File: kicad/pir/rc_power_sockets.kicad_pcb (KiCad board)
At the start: 2 copper layers, 50 x 50 mm, 31 parts, among them IC1 ATTINY85, J1 PIR, J2 433MHZ, J3 433MHZ, P1 ICSP, P2 ALT_PWR, Q1 NMOS, Q2 PMOS, U1 MCP1755ST-3302E/DB

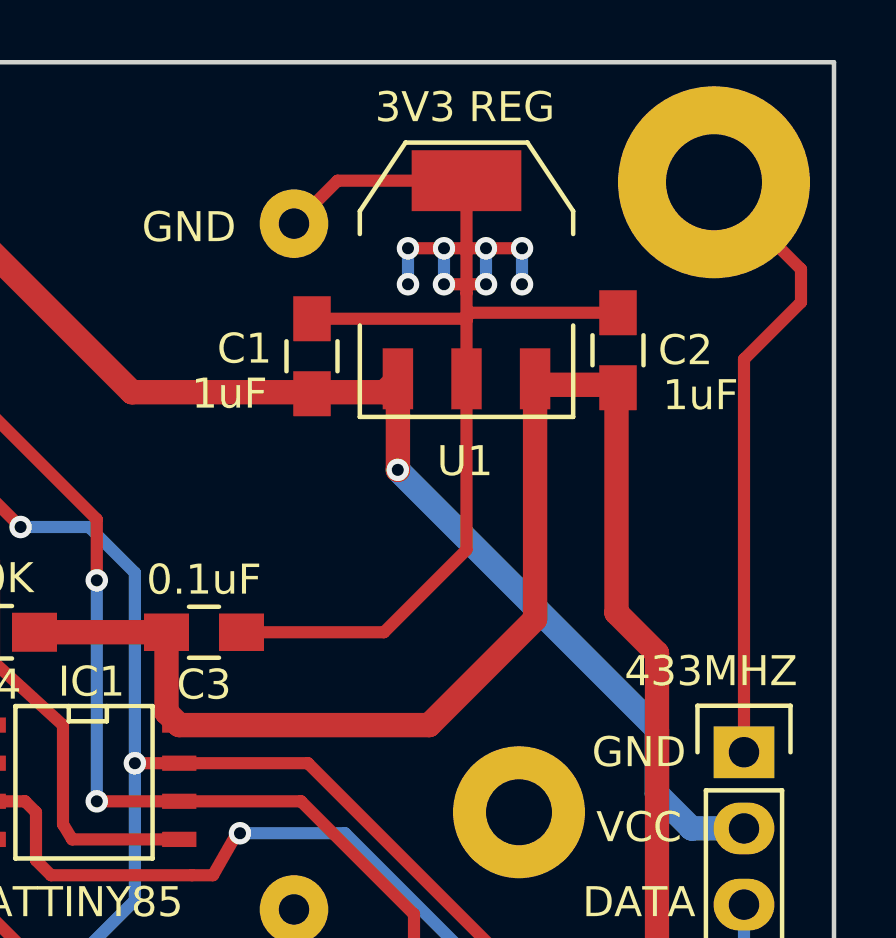
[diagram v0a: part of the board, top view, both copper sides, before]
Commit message: Moved cap away from mounting hole
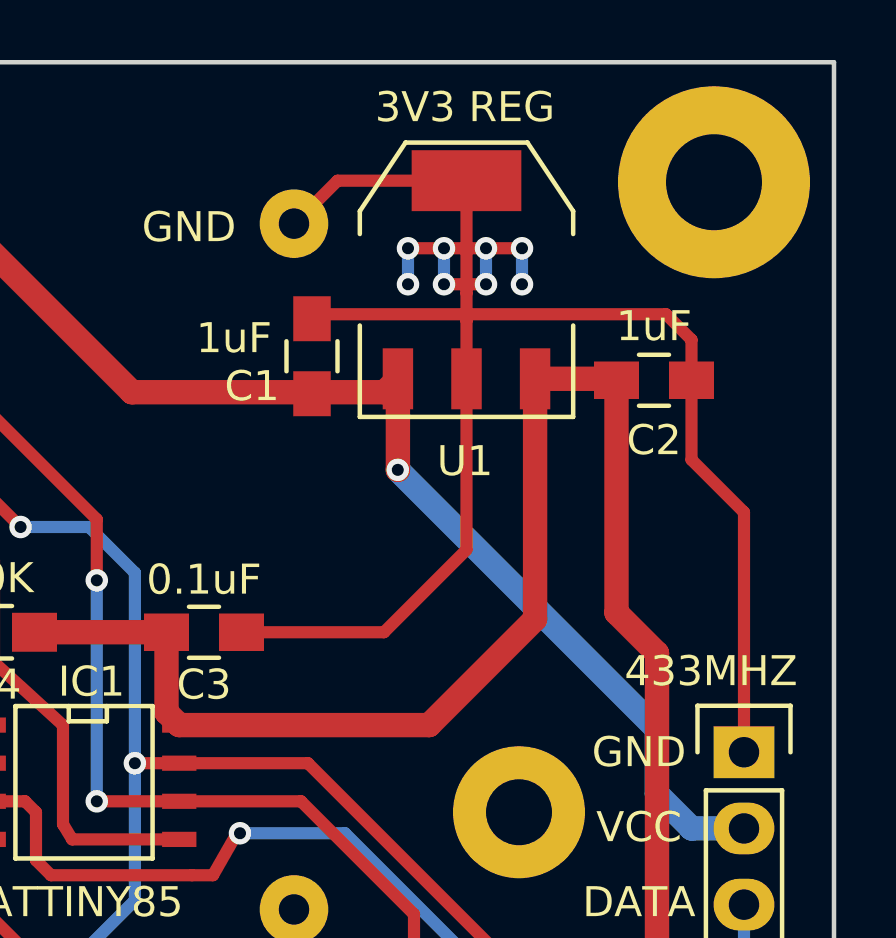
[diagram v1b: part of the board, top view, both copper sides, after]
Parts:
- moved C2 1.56 mm to (164.0, 70.6), turned to 0 degrees
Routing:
- net GND: track 209.1 -> 205.8 mm
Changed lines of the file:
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@@
-(kicad_pcb (version 4) (host pcbnew 4.0.1-stable)
+(kicad_pcb (version 4) (host pcbnew 4.0.2-4+6225~38~ubuntu14.04.1-stable)
   (general
     (links 56)
@@
     (thickness 1.6)
     (drawings 40)
-    (tracks 233)
+    (tracks 235)
     (zones 0)
     (modules 31)
@@
     (tags "capacitor 0805")
     (attr smd)
-    (fp_text reference C1 (at 0.25 -2.25 360) (layer F.SilkS)
-      (effects (font (size 1 1) (thickness 0.15)))
-    )
-    (fp_text value 1uF (at -1.25 -2.75 360) (layer F.SilkS)
+    (fp_text reference C1 (at -1 -2 360) (layer F.SilkS)
+      (effects (font (size 1 1) (thickness 0.15)))
+    )
+    (fp_text value 1uF (at 0.6 -2.6 360) (layer F.SilkS)
       (effects (font (size 1 1) (thickness 0.15)))
     )
@@
   )
   (module Capacitors_SMD:C_0805_HandSoldering (layer F.Cu)
-    (at 162.8 69.6 90)
+    (at 164 70.6)
     (descr "Capacitor SMD 0805, hand soldering")
     (tags "capacitor 0805")
     (attr smd)
-    (fp_text reference C2 (at 0 2.25 360) (layer F.SilkS)
-      (effects (font (size 1 1) (thickness 0.15)))
-    )
-    (fp_text value 1uF (at -1.5 2.75 180) (layer F.SilkS)
+    (fp_text reference C2 (at 0 2) (layer F.SilkS)
+      (effects (font (size 1 1) (thickness 0.15)))
+    )
+    (fp_text value 1uF (at 0 -1.8 180) (layer F.SilkS)
       (effects (font (size 1 1) (thickness 0.15)))
     )
@@
     (fp_line (start 0.5 -0.85) (end -0.5 -0.85) (layer F.SilkS) (width 0.15))
     (fp_line (start -0.5 0.85) (end 0.5 0.85) (layer F.SilkS) (width 0.15))
-    (pad 1 smd rect (at -1.25 0 90) (size 1.5 1.25) (layers F.Cu F.Paste F.Mask)
+    (pad 1 smd rect (at -1.25 0) (size 1.5 1.25) (layers F.Cu F.Paste F.Mask)
       (net 9 /3.3v))
-    (pad 2 smd rect (at 1.25 0 90) (size 1.5 1.25) (layers F.Cu F.Paste F.Mask)
+    (pad 2 smd rect (at 1.25 0) (size 1.5 1.25) (layers F.Cu F.Paste F.Mask)
       (net 1 GND))
     (model Capacitors_SMD.3dshapes/C_0805_HandSoldering.wrl
@@
   (gr_line (start 170 60) (end 170 110) (angle 90) (layer Edge.Cuts) (width 0.15))
   (gr_line (start 120 60) (end 170 60) (angle 90) (layer Edge.Cuts) (width 0.15))
+  (segment (start 157.8 68.4) (end 152.75 68.4) (width 0.406) (layer F.Cu) (net 1) (status 800000))
+  (segment (start 152.75 68.4) (end 152.6 68.55) (width 0.406) (layer F.Cu) (net 1) (status C00000))
+  (segment (start 165.25 70.6) (end 165.25 69.25) (width 0.406) (layer F.Cu) (net 1) (status 400000))
+  (segment (start 164.4 68.4) (end 157.8 68.4) (width 0.406) (layer F.Cu) (net 1))
+  (segment (start 157.8 68.4) (end 157.75 68.4) (width 0.406) (layer F.Cu) (net 1))
+  (segment (start 165.25 69.25) (end 164.4 68.4) (width 0.406) (layer F.Cu) (net 1))
+  (segment (start 167 83) (end 167 75) (width 0.406) (layer F.Cu) (net 1))
+  (segment (start 167 75) (end 165.25 73.25) (width 0.406) (layer F.Cu) (net 1))
+  (segment (start 165.25 73.25) (end 165.25 70.6) (width 0.406) (layer F.Cu) (net 1))
   (segment (start 157 66.2) (end 155.8 66.2) (width 0.406) (layer F.Cu) (net 1))
   (via (at 155.8 66.2) (size 0.75) (drill 0.4) (layers F.Cu B.Cu) (net 1))
@@
   (via (at 158.4 67.4) (size 0.75) (drill 0.4) (layers F.Cu B.Cu) (net 1))
   (segment (start 158.4 67.4) (end 157.75 67.4) (width 0.406) (layer F.Cu) (net 1))
-  (segment (start 162.8 68.35) (end 157.9 68.35) (width 0.406) (layer F.Cu) (net 1))
-  (segment (start 157.9 68.35) (end 157.7 68.55) (width 0.406) (layer F.Cu) (net 1))
-  (segment (start 152.6 68.55) (end 157.7 68.55) (width 0.406) (layer F.Cu) (net 1))
-  (segment (start 157.7 68.55) (end 157.75 68.6) (width 0.406) (layer F.Cu) (net 1))
-  (segment (start 167 83) (end 167 69.9) (width 0.406) (layer F.Cu) (net 1))
-  (segment (start 167 69.9) (end 168.9 68) (width 0.406) (layer F.Cu) (net 1))
-  (segment (start 168.9 68) (end 168.9 66.9) (width 0.406) (layer F.Cu) (net 1))
-  (segment (start 168.9 66.9) (end 166 64) (width 0.406) (layer F.Cu) (net 1))
   (segment (start 141.825 85.905) (end 141.825 88.401) (width 0.406) (layer F.Cu) (net 1))
   (via (at 143.013 89.589) (size 0.75) (drill 0.4) (layers F.Cu B.Cu) (net 1))
@@
   (segment (start 155 79) (end 150.25 79) (width 0.406) (layer F.Cu) (net 1))
   (segment (start 157.75 76.25) (end 155 79) (width 0.406) (layer F.Cu) (net 1))
-  (segment (start 157.75 70.552) (end 157.75 68.6) (width 0.406) (layer F.Cu) (net 1))
+  (segment (start 157.75 70.552) (end 157.75 68.4) (width 0.406) (layer F.Cu) (net 1))
+  (segment (start 157.75 68.4) (end 157.75 68.6) (width 0.406) (layer F.Cu) (net 1))
+  (segment (start 157.75 67.7) (end 157.75 67.4) (width 0.406) (layer F.Cu) (net 1))
   (segment (start 157.75 68.6) (end 157.75 67.7) (width 0.406) (layer F.Cu) (net 1))
-  (segment (start 157.75 67.7) (end 157.75 67.4) (width 0.406) (layer F.Cu) (net 1))
   (segment (start 157.75 67.4) (end 157.75 63.948) (width 0.406) (layer F.Cu) (net 1))
   (segment (start 166 106) (end 166 99) (width 0.406) (layer B.Cu) (net 1))
@@
   (segment (start 137.65 61.55) (end 138.5 62.5) (width 0.813) (layer F.Cu) (net 8))
   (segment (start 138.5 62.5) (end 138.5 64.06) (width 0.813) (layer F.Cu) (net 8))
+  (segment (start 162.75 70.55) (end 162.75 78.35) (width 0.813) (layer F.Cu) (net 9))
+  (segment (start 162.75 78.35) (end 164.1 79.7) (width 0.813) (layer F.Cu) (net 9))
+  (segment (start 164.1 79.7) (end 164.1 92.02) (width 0.813) (layer F.Cu) (net 9))
   (segment (start 147.75 79) (end 147.75 81.67) (width 0.813) (layer F.Cu) (net 9))
   (segment (start 147.75 81.67) (end 148.175 82.095) (width 0.813) (layer F.Cu) (net 9))
-  (segment (start 162.75 70.75) (end 162.75 78.35) (width 0.813) (layer F.Cu) (net 9))
   (segment (start 164.1 92.02) (end 166 93.92) (width 0.813) (layer F.Cu) (net 9))
-  (segment (start 164.1 79.7) (end 164.1 92.02) (width 0.813) (layer F.Cu) (net 9))
-  (segment (start 162.75 78.35) (end 164.1 79.7) (width 0.813) (layer F.Cu) (net 9))
   (segment (start 160.036 70.552) (end 160.036 78.564) (width 0.813) (layer F.Cu) (net 9))
   (segment (start 156.505 82.095) (end 148.175 82.095) (width 0.813) (layer F.Cu) (net 9))
   (segment (start 160.036 78.564) (end 156.505 82.095) (width 0.813) (layer F.Cu) (net 9))
-  (segment (start 162.75 70.75) (end 160.234 70.75) (width 0.813) (layer F.Cu) (net 9))
-  (segment (start 160.234 70.75) (end 160.036 70.552) (width 0.813) (layer F.Cu) (net 9))
+  (segment (start 162.75 70.55) (end 160.034 70.55) (width 0.813) (layer F.Cu) (net 9))
+  (segment (start 160.034 70.55) (end 160.036 70.552) (width 0.813) (layer F.Cu) (net 9))
   (segment (start 147.75 79) (end 143.35 79) (width 0.813) (layer F.Cu) (net 9))
   (segment (start 154.65 99) (end 152.906 99) (width 0.406) (layer F.Cu) (net 10))

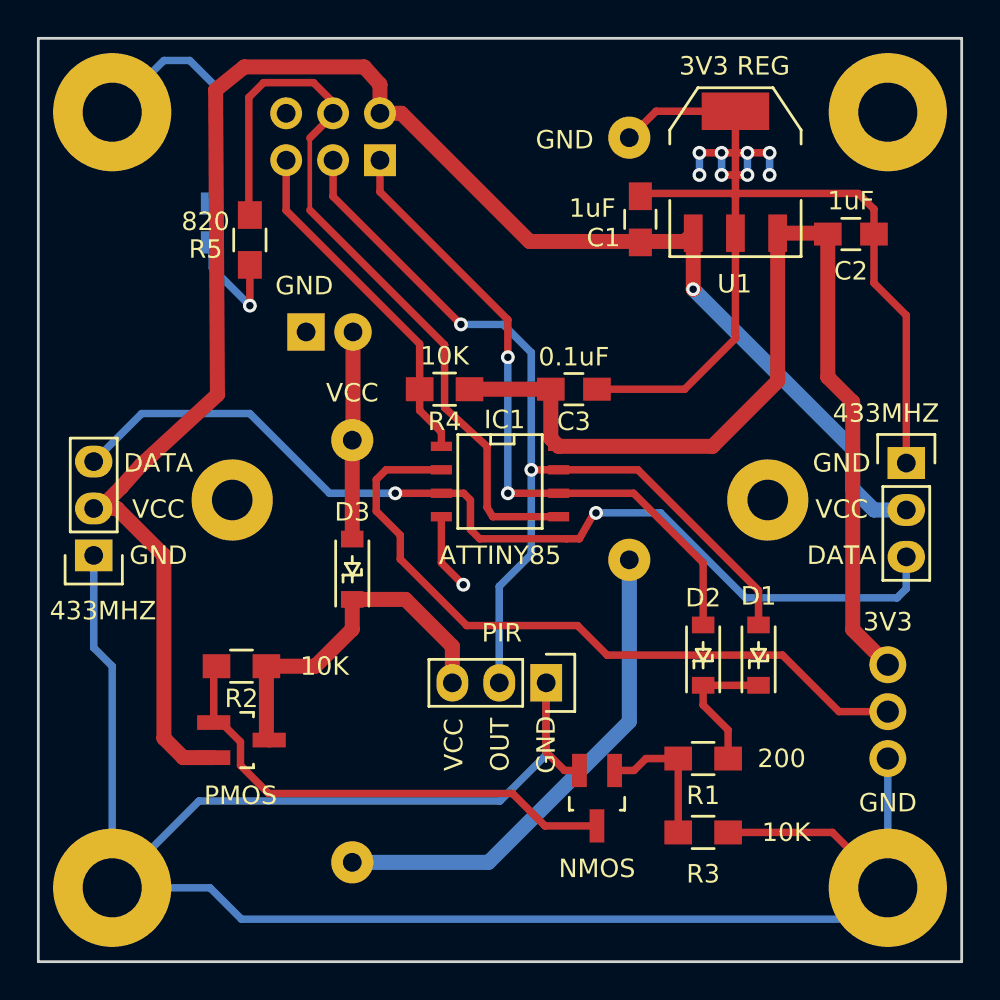
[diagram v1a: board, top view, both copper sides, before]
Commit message: 20mm pin to pin for CR2032 holder
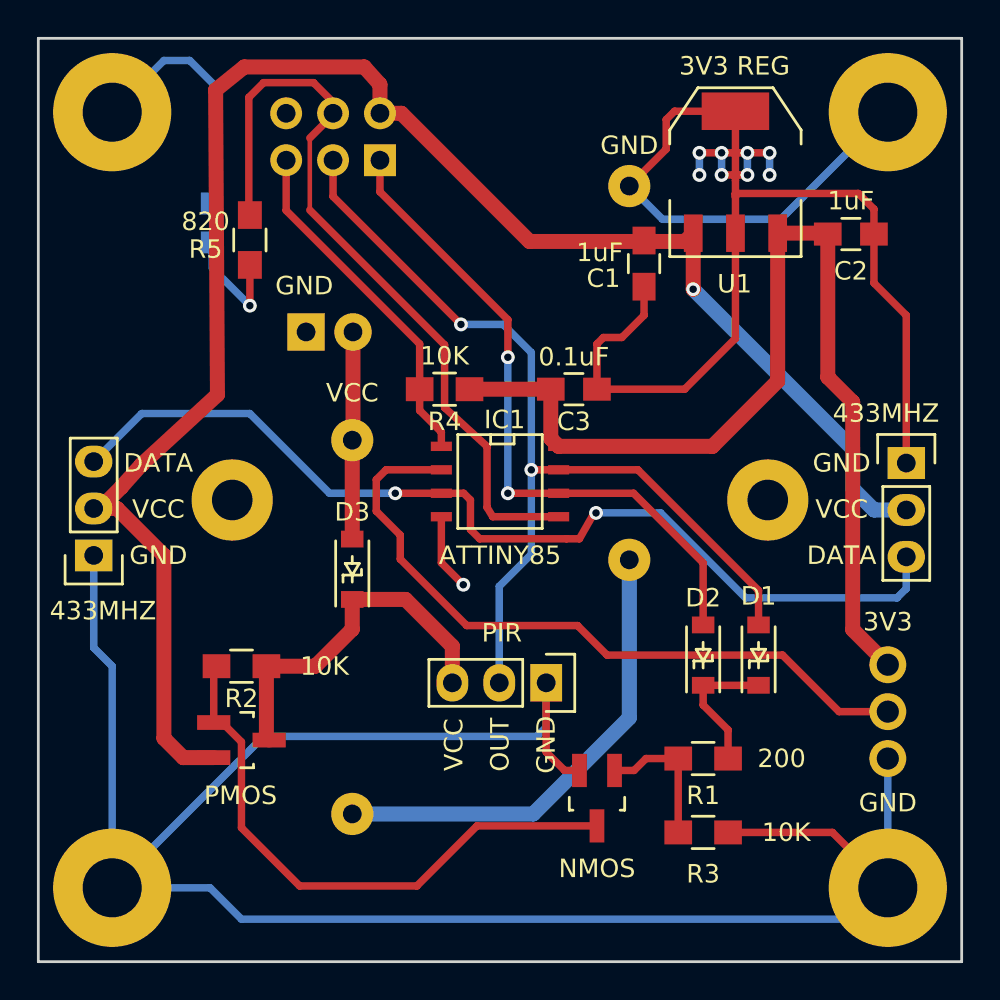
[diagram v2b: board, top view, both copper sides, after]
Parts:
- moved C1 2.41 mm to (152.8, 72.2), turned to 270 degrees
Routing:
- net GND: track 205.8 -> 221.4 mm
- net /PBASE: track 27.5 -> 32.6 mm
- net /BATT: track 26.9 -> 25.7 mm
